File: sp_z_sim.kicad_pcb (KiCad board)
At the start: 4 copper layers, 124 x 47 mm, 120 parts, among them J1 USB_B_Micro, J10 ADC_EXTRA, J11 IN+, J12 IN-, J13 CAL_3.3, J14 CAL_3.3, J15 FAN, J2 TEMP1, J3 TEMP1, J4 SWD, J5 Micro_SD_Card_Det, J6 OUT1, J7 OUT2, J8 4T_1, J9 4T_2, Q1 Q_NMOS_GSD, Q2 Q_NMOS_GSD, Q3 Q_NMOS_GSD, Q4 Q_NMOS_GSD, Q5 Q_NMOS_GSD, Q6 Q_NMOS_GSD, U1 OPA549, U10 AZ1117-3.3, U2 INA240A1PW, U3 OPA549, U4 INA240A1PW, U5 PDS760-13, U6 TPS54561DPRR, U7 STM32F405RGTx, U8 ADR4533BRZ, U9 TPS54160, Y1 Crystal_GND24

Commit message: Updated solder mask settings
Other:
- rule pad_to_mask_clearance: 0.051 -> 0.02
- rule solder_mask_min_width: 0.25 -> 0.2

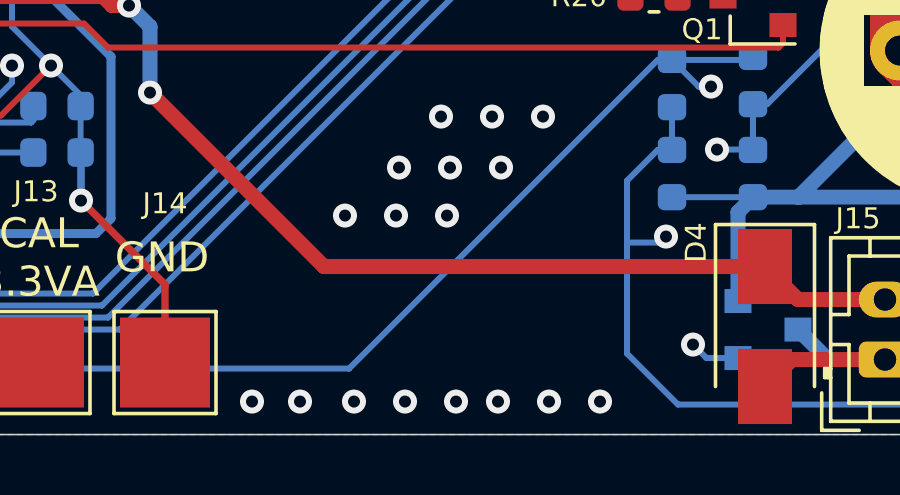
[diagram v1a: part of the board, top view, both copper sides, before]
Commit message: Added PCB name to silkscreen
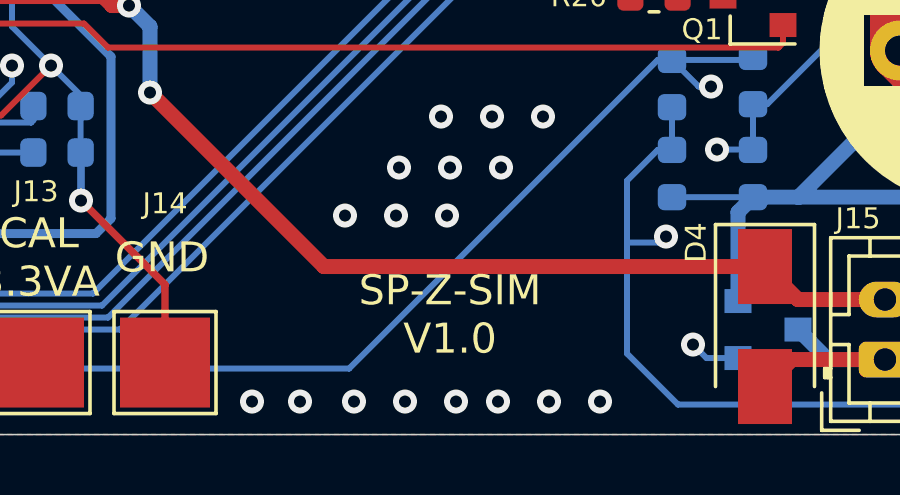
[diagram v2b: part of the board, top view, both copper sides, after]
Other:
- board text added: "SP-Z-SIM V1.0"

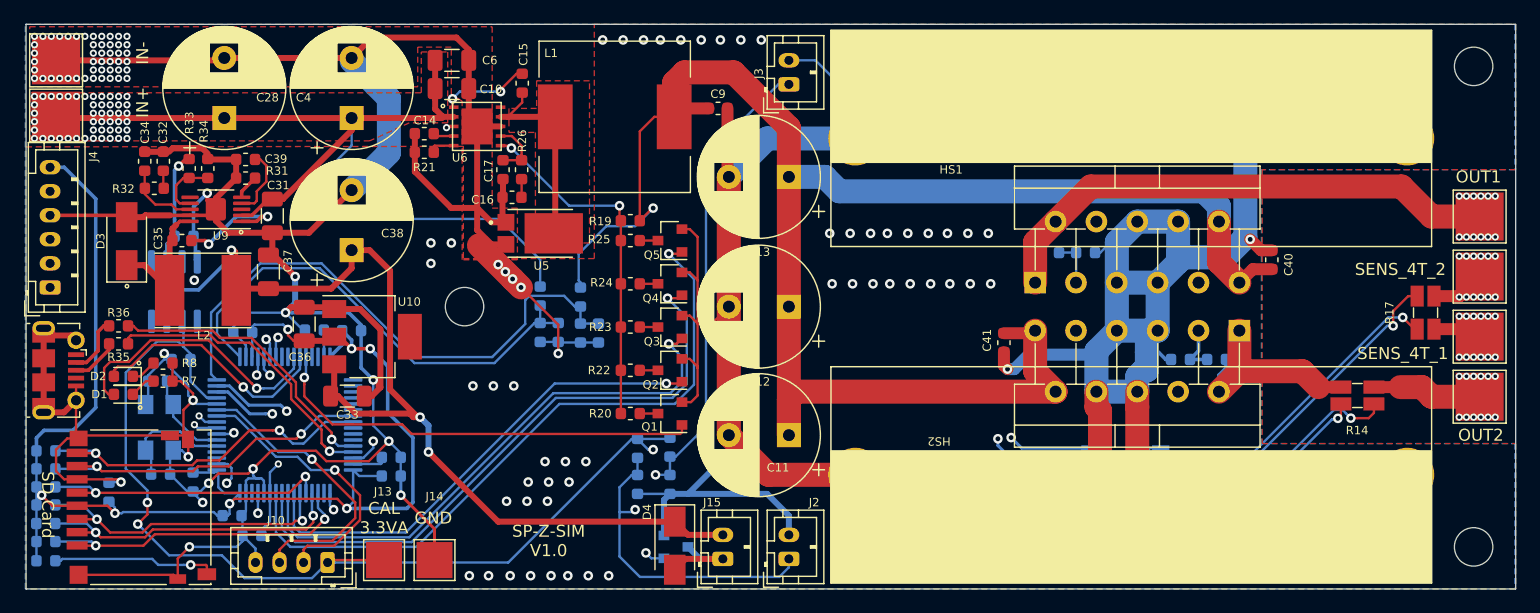
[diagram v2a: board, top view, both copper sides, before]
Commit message: Added testpoints, changed connectors, changed shunts
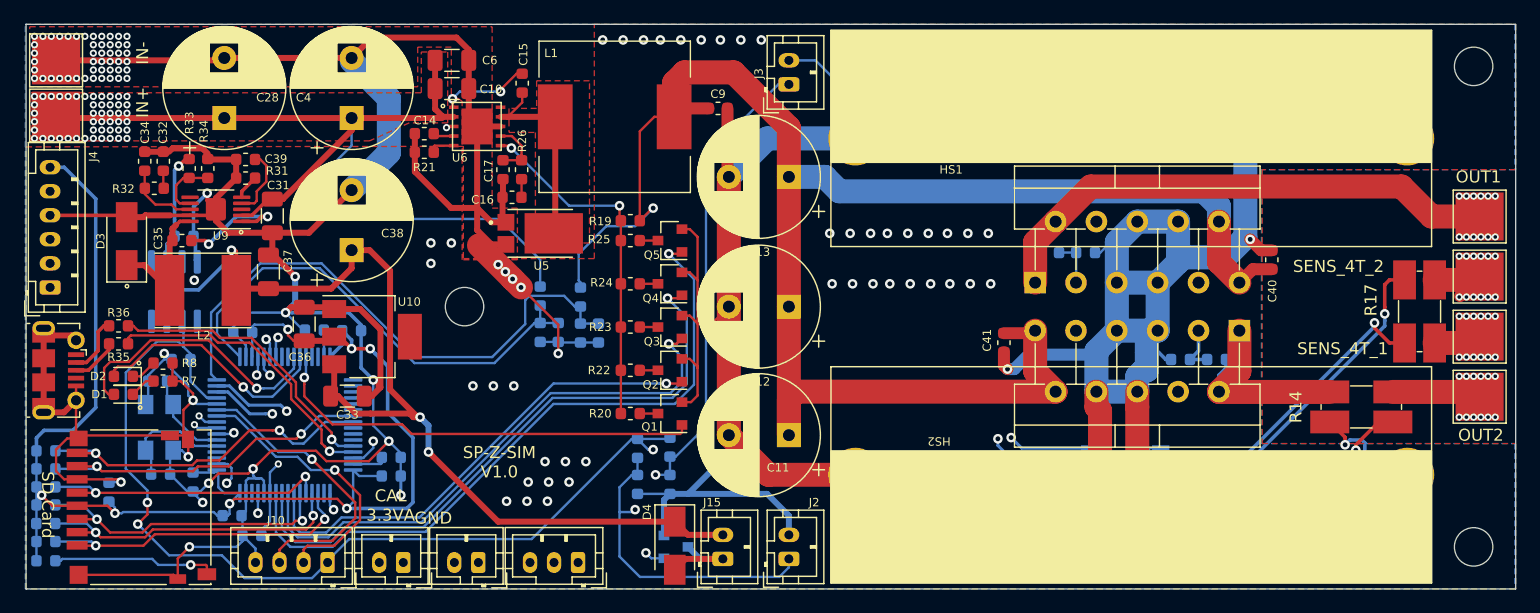
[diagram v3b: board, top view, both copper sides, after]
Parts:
- added J16: TP_AMP, Connector_JST:JST_PH_B3B-PH-K_1x03_P2.00mm_Vertical, F.Cu at (176.9, 91.3)
- C20, C21: value 22p -> 15p
- C35: value 100n -> 0.1u
- J13: footprint TestPoint:TestPoint_Pad_3.0x3.0mm -> Connector_JST:JST_PH_B2B-PH-K_1x02_P2.00mm_Vertical
- J14: value CAL_3.3 -> TP_DAC; footprint TestPoint:TestPoint_Pad_3.0x3.0mm -> Connector_JST:JST_PH_B2B-PH-K_1x02_P2.00mm_Vertical
- R14, R17: footprint Resistor_SMD:R_Shunt_Ohmite_LVK12 -> Resistor_SMD:R_Shunt_Ohmite_LVK24
- moved J14 3.66 mm to (168.7, 91.3), turned to 180 degrees
- moved J13 1.61 mm to (162.4, 91.3), turned to 180 degrees
- moved R14 1.00 mm to (242.2, 78.3)
- moved R17 0.51 mm to (247.0, 70.4)
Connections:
- net /PA0_SHUNT1 renamed /TP_I1
- net /PA1_SHUNT2 renamed /TP_I2
- net /PA3_DCDC_IN renamed /PWR_DIV
- net /PB5_VSEL_4 renamed /VSEL4
- net /PB6_VSEL_5 renamed /VSEL5
- net /PB7_OUT_EN renamed /ENABLE
- J14 pad 1: GND -> /TP_DAC1
- U1 pad 4: /PA4_DAC1 -> /TP_DAC1
- U3 pad 4: /PA5_DAC2 -> /TP_DAC2
- U7 pad 20: /PA4_DAC1 -> /TP_DAC1
- U7 pad 21: /PA5_DAC2 -> /TP_DAC2
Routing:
- net /TP_DAC1: track 0.00 -> 85.3 mm, vias 0 -> 1
- net /PA4_DAC1: track 85.3 -> 0.00 mm, vias 1 -> 0
- net /TP_DAC2: track 0.00 -> 79.3 mm, vias 0 -> 1
- net /PA5_DAC2: track 79.3 -> 0.00 mm, vias 1 -> 0
- net GND: track 728.3 -> 721.7 mm, vias 166 -> 158
- net Net-(R14-Pad4): track 20.0 -> 25.0 mm
- net +3.3VA: track 143.7 -> 139.0 mm
- net /OUT1: track 9.13 -> 7.39 mm
- net /SENSE_4T_1: track 4.47 -> 6.16 mm
- net Net-(R17-Pad4): track 27.8 -> 28.6 mm
- net /SENSE_4T_2: track 4.06 -> 4.85 mm
- net Net-(R17-Pad2): track 26.7 -> 26.0 mm

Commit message: Finished routing and added gerber files
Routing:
- net GND: track 721.7 -> 744.9 mm
- net /TP_DAC2: track 79.3 -> 100.2 mm, vias 1 -> 2
- net /TP_DAC1: track 85.3 -> 105.6 mm, vias 1 -> 2
- net /TP_I2: track 76.3 -> 90.3 mm, vias 2 -> 3
- net /TP_I1: track 79.0 -> 90.5 mm, vias 2 -> 3
- net /PB2_VSEL_1: track 36.7 -> 40.4 mm
- net +3.3VA: track 139.0 -> 142.2 mm
- net /PB3_VSEL_2: track 40.5 -> 41.3 mm
- net +5V: track 92.6 -> 92.0 mm
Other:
- board text added: "DAC1"
- board text added: "DAC2"
- board text added: "EXTRA"
- board text added: "I1"
- board text added: "I2"
- board text added: "SWD"
- board text added: "T1"
- board text added: "T2"
- board text added: "TP AMP"
- board text added: "TP DAC"

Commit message: Changed fan mosfet part number
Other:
- rule solder_mask_min_width: 0.2 -> 0.1
